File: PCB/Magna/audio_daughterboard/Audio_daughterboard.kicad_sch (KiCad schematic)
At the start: 26 parts, among them U201 24.576 MHz, U202 CY2305SXC-1HT, U203 CY2305SXC-1HT

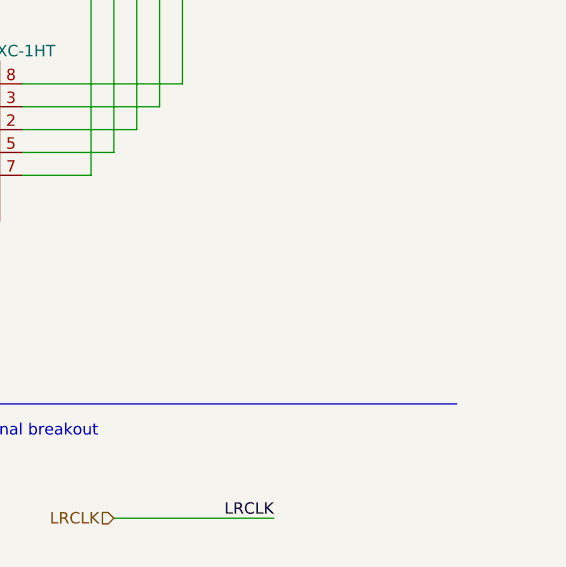
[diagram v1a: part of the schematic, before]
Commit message: Move VAA circuitry to Analogue daughterboard (#11)
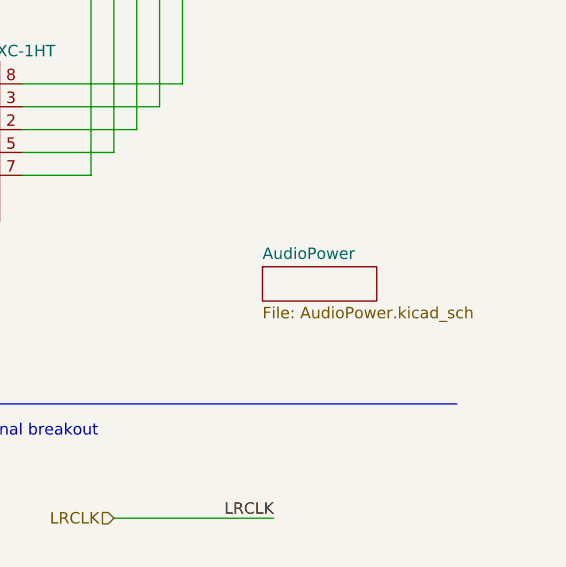
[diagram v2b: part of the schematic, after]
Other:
- added sheet AudioPower (AudioPower.kicad_sch)
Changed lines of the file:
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@@
       (project "Audio_daughterboard"
         (path "/1eadd930-2484-4c28-b568-78e6454e7f52"
-          (reference "U203") (unit 1)
+          (reference "U103") (unit 1)
         )
       )
@@
       (project "Audio_daughterboard"
         (path "/1eadd930-2484-4c28-b568-78e6454e7f52"
-          (reference "TP205") (unit 1)
+          (reference "TP105") (unit 1)
         )
       )
@@
       (project "Audio_daughterboard"
         (path "/1eadd930-2484-4c28-b568-78e6454e7f52"
-          (reference "#PWR0205") (unit 1)
+          (reference "#PWR0105") (unit 1)
         )
       )
@@
       (project "Audio_daughterboard"
         (path "/1eadd930-2484-4c28-b568-78e6454e7f52"
-          (reference "JP204") (unit 1)
+          (reference "JP104") (unit 1)
         )
       )
@@
       (project "Audio_daughterboard"
         (path "/1eadd930-2484-4c28-b568-78e6454e7f52"
-          (reference "#PWR0206") (unit 1)
+          (reference "#PWR0106") (unit 1)
         )
       )
@@
       (project "Audio_daughterboard"
         (path "/1eadd930-2484-4c28-b568-78e6454e7f52"
-          (reference "JP203") (unit 1)
+          (reference "JP103") (unit 1)
         )
       )
@@
       (project "Audio_daughterboard"
         (path "/1eadd930-2484-4c28-b568-78e6454e7f52"
-          (reference "JP210") (unit 1)
+          (reference "JP110") (unit 1)
         )
       )
@@
       (project "Audio_daughterboard"
         (path "/1eadd930-2484-4c28-b568-78e6454e7f52"
-          (reference "R201") (unit 1)
+          (reference "R101") (unit 1)
         )
       )
@@
       (project "Audio_daughterboard"
         (path "/1eadd930-2484-4c28-b568-78e6454e7f52"
-          (reference "#PWR0208") (unit 1)
+          (reference "#PWR0108") (unit 1)
         )
       )
@@
       (project "Audio_daughterboard"
         (path "/1eadd930-2484-4c28-b568-78e6454e7f52"
-          (reference "JP209") (unit 1)
+          (reference "JP109") (unit 1)
         )
       )
@@
       (project "Audio_daughterboard"
         (path "/1eadd930-2484-4c28-b568-78e6454e7f52"
-          (reference "TP208") (unit 1)
+          (reference "TP108") (unit 1)
         )
       )
@@
       (project "Audio_daughterboard"
         (path "/1eadd930-2484-4c28-b568-78e6454e7f52"
-          (reference "#PWR0204") (unit 1)
+          (reference "#PWR0104") (unit 1)
         )
       )
@@
       (project "Audio_daughterboard"
         (path "/1eadd930-2484-4c28-b568-78e6454e7f52"
-          (reference "TP203") (unit 1)
+          (reference "TP103") (unit 1)
         )
       )
@@
       (project "Audio_daughterboard"
         (path "/1eadd930-2484-4c28-b568-78e6454e7f52"
-          (reference "JP207") (unit 1)
+          (reference "JP107") (unit 1)
         )
       )
@@
       (project "Audio_daughterboard"
         (path "/1eadd930-2484-4c28-b568-78e6454e7f52"
-          (reference "TP204") (unit 1)
+          (reference "TP104") (unit 1)
         )
       )
@@
       (project "Audio_daughterboard"
         (path "/1eadd930-2484-4c28-b568-78e6454e7f52"
-          (reference "#PWR0203") (unit 1)
+          (reference "#PWR0103") (unit 1)
         )
       )
@@
       (project "Audio_daughterboard"
         (path "/1eadd930-2484-4c28-b568-78e6454e7f52"
-          (reference "TP207") (unit 1)
+          (reference "TP107") (unit 1)
         )
       )
@@
       (project "Audio_daughterboard"
         (path "/1eadd930-2484-4c28-b568-78e6454e7f52"
-          (reference "TP201") (unit 1)
+          (reference "TP101") (unit 1)
         )
       )
@@
       (project "Audio_daughterboard"
         (path "/1eadd930-2484-4c28-b568-78e6454e7f52"
-          (reference "JP206") (unit 1)
+          (reference "JP106") (unit 1)
         )
       )
@@
       (project "Audio_daughterboard"
         (path "/1eadd930-2484-4c28-b568-78e6454e7f52"
-          (reference "TP210") (unit 1)
+          (reference "TP110") (unit 1)
         )
       )
@@
       (project "Audio_daughterboard"
         (path "/1eadd930-2484-4c28-b568-78e6454e7f52"
-          (reference "JP201") (unit 1)
+          (reference "JP101") (unit 1)
         )
       )
@@
       (project "Audio_daughterboard"
         (path "/1eadd930-2484-4c28-b568-78e6454e7f52"
-          (reference "TP206") (unit 1)
+          (reference "TP106") (unit 1)
         )
       )
@@
       (project "Audio_daughterboard"
         (path "/1eadd930-2484-4c28-b568-78e6454e7f52"
-          (reference "R202") (unit 1)
+          (reference "R102") (unit 1)
         )
       )
@@
       (project "Audio_daughterboard"
         (path "/1eadd930-2484-4c28-b568-78e6454e7f52"
-          (reference "#PWR0207") (unit 1)
+          (reference "#PWR0107") (unit 1)
         )
       )
@@
       (project "Audio_daughterboard"
         (path "/1eadd930-2484-4c28-b568-78e6454e7f52"
-          (reference "C201") (unit 1)
+          (reference "C101") (unit 1)
         )
       )
@@
       (project "Audio_daughterboard"
         (path "/1eadd930-2484-4c28-b568-78e6454e7f52"
-          (reference "#PWR0209") (unit 1)
+          (reference "#PWR0109") (unit 1)
         )
       )
@@
       (project "Audio_daughterboard"
         (path "/1eadd930-2484-4c28-b568-78e6454e7f52"
-          (reference "U201") (unit 1)
+          (reference "U101") (unit 1)
         )
       )
@@
       (project "Audio_daughterboard"
         (path "/1eadd930-2484-4c28-b568-78e6454e7f52"
-          (reference "JP202") (unit 1)
+          (reference "JP102") (unit 1)
         )
       )
@@
       (project "Audio_daughterboard"
         (path "/1eadd930-2484-4c28-b568-78e6454e7f52"
-          (reference "JP205") (unit 1)
+          (reference "JP105") (unit 1)
         )
       )
@@
       (project "Audio_daughterboard"
         (path "/1eadd930-2484-4c28-b568-78e6454e7f52"
-          (reference "#PWR0202") (unit 1)
+          (reference "#PWR0102") (unit 1)
         )
       )
@@
       (project "Audio_daughterboard"
         (path "/1eadd930-2484-4c28-b568-78e6454e7f52"
-          (reference "TP209") (unit 1)
+          (reference "TP109") (unit 1)
         )
       )
@@
       (project "Audio_daughterboard"
         (path "/1eadd930-2484-4c28-b568-78e6454e7f52"
-          (reference "#PWR0201") (unit 1)
+          (reference "#PWR0101") (unit 1)
         )
       )
@@
       (project "Audio_daughterboard"
         (path "/1eadd930-2484-4c28-b568-78e6454e7f52"
-          (reference "JP208") (unit 1)
+          (reference "JP108") (unit 1)
         )
       )
@@
       (project "Audio_daughterboard"
         (path "/1eadd930-2484-4c28-b568-78e6454e7f52"
-          (reference "U202") (unit 1)
+          (reference "U102") (unit 1)
         )
       )
@@
       (project "Audio_daughterboard"
         (path "/1eadd930-2484-4c28-b568-78e6454e7f52"
-          (reference "TP202") (unit 1)
+          (reference "TP102") (unit 1)
         )
       )
@@
       )
     )
+  )
+  (sheet (at 262.89 101.6) (size 12.7 3.81) (fields_autoplaced)
+    (stroke (width 0.1524) (type solid))
+    (fill (color 0 0 0 0.0000))
+    (property "Sheetname" "AudioPower" (at 262.89 100.8884 0)
+      (effects (font (size 1.27 1.27)) (justify left bottom))
+    )
+    (property "Sheetfile" "AudioPower.kicad_sch" (at 262.89 105.9946 0)
+      (effects (font (size 1.27 1.27)) (justify left top))
+    )
+    (instances
+      (project "Audio_daughterboard"
+        (path "/1eadd930-2484-4c28-b568-78e6454e7f52" (page "9"))
+      )
+    )

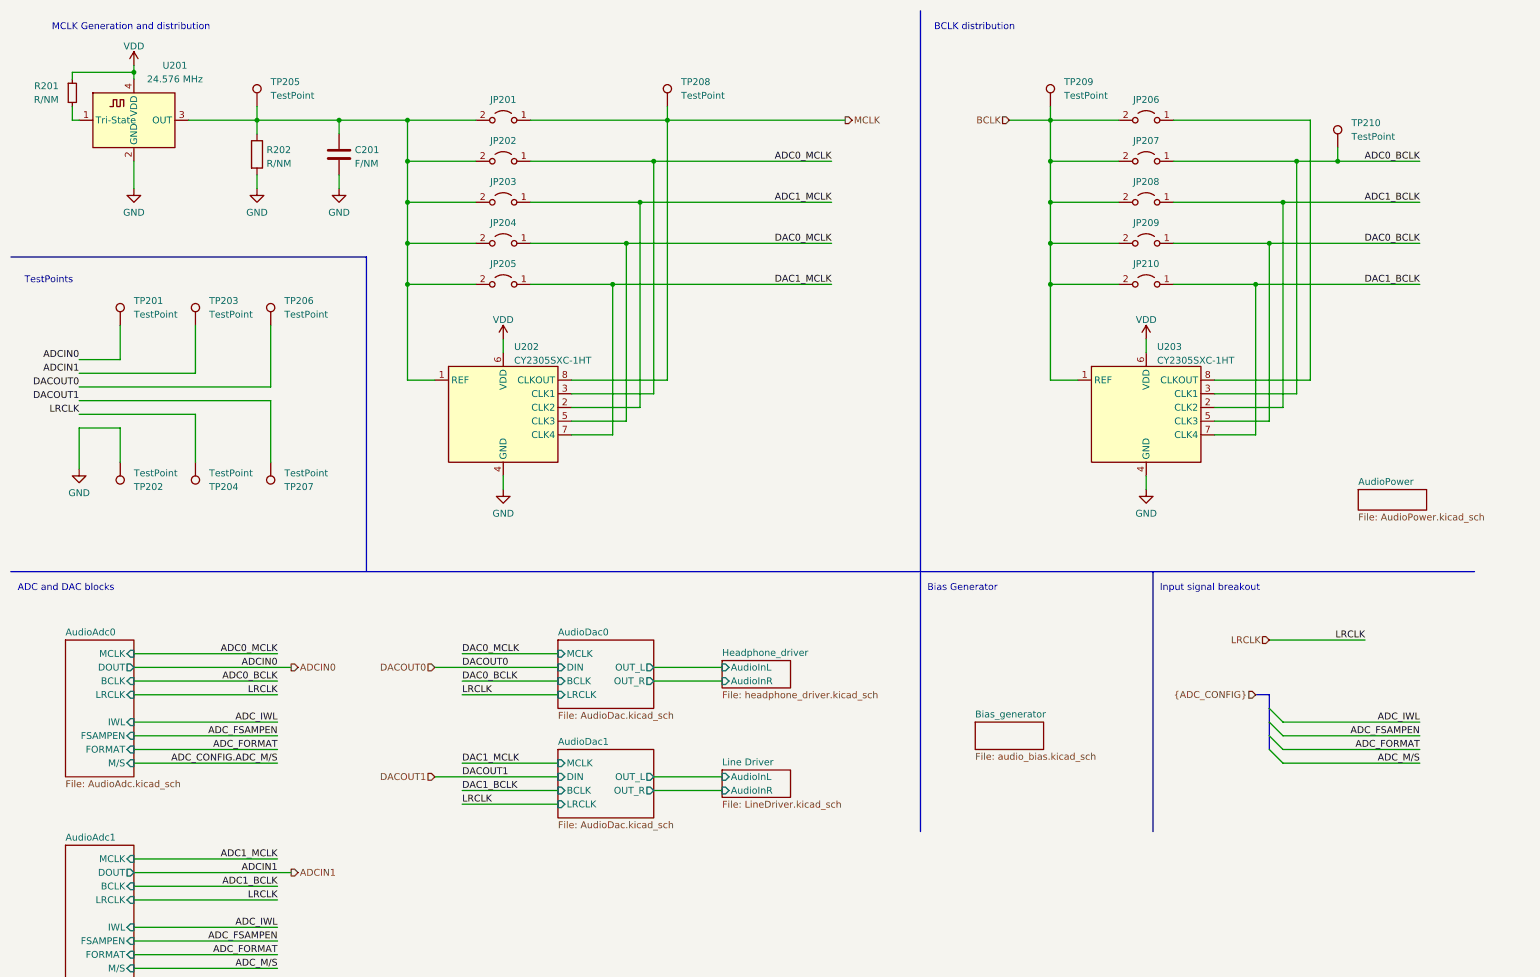
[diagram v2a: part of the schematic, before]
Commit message: Update connector on ADC board and clean up MCU sheet
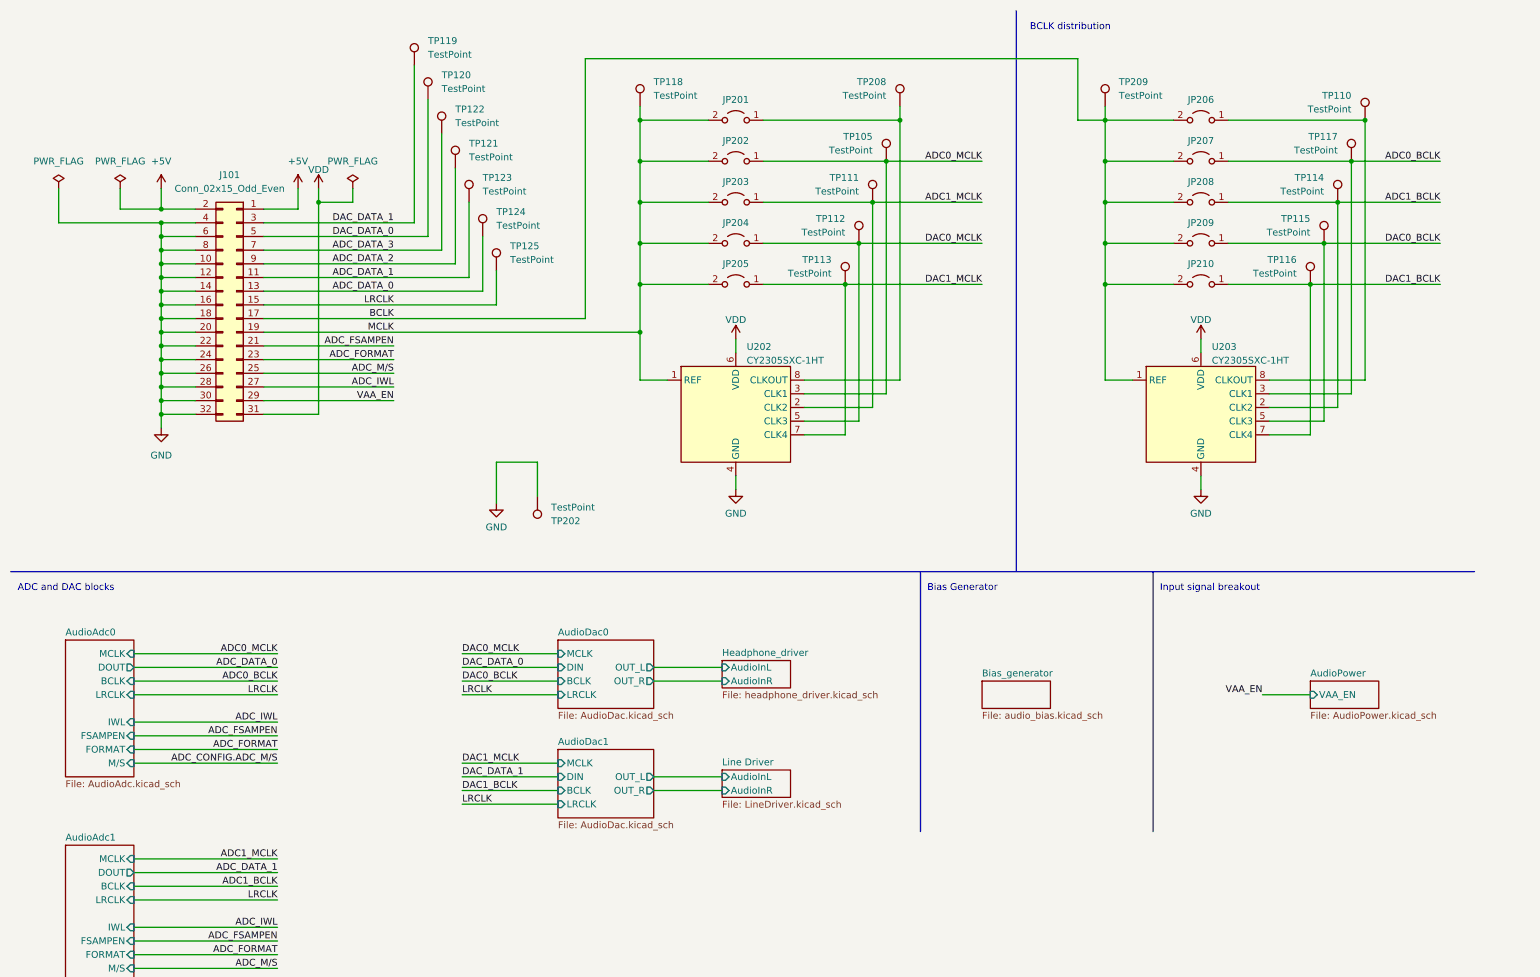
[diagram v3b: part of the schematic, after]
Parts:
- removed C201: F/NM, Capacitor_SMD:C_0603_1608Metric_Pad1.08x0.95mm_HandSolder, symbol Device:C
- removed R201: R/NM, Resistor_SMD:R_0805_2012Metric_Pad1.20x1.40mm_HandSolder, symbol Device:R_Small
- removed R202: R/NM, Resistor_SMD:R_0805_2012Metric_Pad1.20x1.40mm_HandSolder, symbol Device:R
- removed TP201, TP203, TP204, TP205, TP206, TP207, TP210: TestPoint, TestPoint:TestPoint_Keystone_5005-5009_Compact, symbol Connector:TestPoint
- removed U201: 24.576 MHz, Oscillator:Oscillator_SMD_Abracon_ASE-4Pin_3.2x2.5mm_HandSoldering, symbol Oscillator:ECS-2520MV-xxx-xx
- added J101: Conn_02x15_Odd_Even, Connector_PinHeader_2.54mm:PinHeader_2x16_P2.54mm_Horizontal, symbol Connector_Generic:Conn_02x16_Odd_Even
- added TP105, TP110, TP111, TP112, TP113, TP114, TP115, TP116, TP117, TP118, TP119, TP120, TP121, TP122, TP123, TP124, TP125: TestPoint, TestPoint:TestPoint_Keystone_5005-5009_Compact, symbol Connector:TestPoint
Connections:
- net ADC0_BCLK: now also TP117.1
- net ADC0_MCLK: now also TP105.1
- net ADC1_BCLK: now also TP114.1
- net ADC1_MCLK: now also TP111.1
- net ADC_FORMAT: now also J101.23 (Pin_23)
- net ADC_FSAMPEN: now also J101.21 (Pin_21)
- net ADC_IWL: now also J101.27 (Pin_27)
- net ADC_M/S: now also J101.25 (Pin_25)
- net BCLK: now also J101.17 (Pin_17)
- net DAC0_BCLK: now also TP115.1
- net DAC0_MCLK: now also TP112.1
- net DAC1_BCLK: now also TP116.1
- net DAC1_MCLK: now also TP113.1
- net GND: now also J101.10 (Pin_10), J101.12 (Pin_12), J101.14 (Pin_14), J101.16 (Pin_16), J101.18 (Pin_18), J101.20 (Pin_20), J101.22 (Pin_22), J101.24 (Pin_24), J101.26 (Pin_26), J101.28 (Pin_28), J101.30 (Pin_30), J101.32 (Pin_32), J101.4 (Pin_4), J101.6 (Pin_6), J101.8 (Pin_8)
- net LRCLK: now also J101.15 (Pin_15), TP125.1
- net MCLK: now also JP201.2 (B), JP202.2 (B), JP203.2 (B), JP204.2 (B), JP205.2 (B), U202.1 (REF), J101.19 (Pin_19), TP118.1; no longer JP201.1 (A), TP208.1, U202.8 (CLKOUT)
- net VDD: now also J101.31 (Pin_31)
- net at JP206.1 (A), U203.8 (CLKOUT): now also TP110.1
- new net: JP201.1 (A), TP208.1, U202.8 (CLKOUT)
- new net +5V: J101.1 (Pin_1), J101.2 (Pin_2)
- new net ADC_DATA_0: J101.13 (Pin_13), TP124.1
- new net ADC_DATA_1: J101.11 (Pin_11), TP123.1
- new net ADC_DATA_2: J101.9 (Pin_9), TP121.1
- new net ADC_DATA_3: J101.7 (Pin_7), TP122.1
- new net DAC_DATA_0: J101.5 (Pin_5), TP120.1
- new net DAC_DATA_1: J101.3 (Pin_3), TP119.1
- new net VAA_EN: J101.29 (Pin_29)
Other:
- sheet AudioPower ports: added VAA_EN; removed none
- note removed: "MCLK Generation and distribution"
- note removed: "TestPoints"
- moved on the sheet: JP201, JP202, JP203, JP204, JP205, JP206, JP207, JP208, JP209, JP210, TP202, TP208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
